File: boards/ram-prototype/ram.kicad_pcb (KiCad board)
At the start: 4 copper layers, 158 x 141 mm, 630 parts, among them J1 PinHeader_1x24_P2.54mm_Vertic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, J2 PinHeader_1x04_P2.54mm_Vertic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, J3 PinHeader_1x14_P2.54mm_Vertic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, J4 PinHeader_1x16_P2.54mm_Vertic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, J5 Molex_Mini-Fit_Jr_5566-08A_2x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, U1 DSBGA\-5_NumericPads, U10 DSBGA\-5_NumericPads, U100 DSBGA\-5_NumericPads, U101 DSBGA\-5_NumericPads, U102 DSBGA\-5_NumericPads, U103 DSBGA\-5_NumericPads, U104 DSBGA\-5_NumericPads, U105 DSBGA\-5_NumericPads, U106 DSBGA\-5_NumericPads, U107 DSBGA\-5_NumericPads, U108 DSBGA\-5_NumericPads, U109 DSBGA\-5_NumericPads, U11 DSBGA\-5_NumericPads, U110 DSBGA\-5_NumericPads, U111 DSBGA\-5_NumericPads, U112 DSBGA\-5_NumericPads, U113 DSBGA\-5_NumericPads, U114 DSBGA\-5_NumericPads, U115 DSBGA\-5_NumericPads, U116 DSBGA\-5_NumericPads, U117 DSBGA\-5_NumericPads, U118 DSBGA\-5_NumericPads, U119 DSBGA\-5_NumericPads, U12 DSBGA\-5_NumericPads, U120 DSBGA\-5_NumericPads, U121 DSBGA\-5_NumericPads, U122 DSBGA\-5_NumericPads, U123 DSBGA\-5_NumericPads, U124 DSBGA\-5_NumericPads, U125 DSBGA\-5_NumericPads, U126 DSBGA\-5_NumericPads, U127 DSBGA\-5_NumericPads, U128 DSBGA\-5_NumericPads, U129 DSBGA\-5_NumericPads, U13 DSBGA\-5_NumericPads, U130 DSBGA\-5_NumericPads, U131 DSBGA\-5_NumericPads, U132 DSBGA\-5_NumericPads, U133 DSBGA\-5_NumericPads, U134 DSBGA\-5_NumericPads, U135 DSBGA\-5_NumericPads, U136 DSBGA\-5_NumericPads, U137 DSBGA\-5_NumericPads, U138 DSBGA\-5_NumericPads, U139 DSBGA\-5_NumericPads, U14 DSBGA\-5_NumericPads, U140 DSBGA\-5_NumericPads, U141 DSBGA\-5_NumericPads, U142 DSBGA\-5_NumericPads, U143 DSBGA\-5_NumericPads, U144 DSBGA\-5_NumericPads, U145 DSBGA\-5_NumericPads, U146 DSBGA\-5_NumericPads, U147 DSBGA\-5_NumericPads, U148 DSBGA\-5_NumericPads, U149 DSBGA\-5_NumericPads, U15 DSBGA\-5_NumericPads, U150 DSBGA\-5_NumericPads, U151 DSBGA\-5_NumericPads, U152 DSBGA\-5_NumericPads, U153 DSBGA\-5_NumericPads, U154 DSBGA\-5_NumericPads, U155 DSBGA\-5_NumericPads, U156 DSBGA\-5_NumericPads, U157 DSBGA\-5_NumericPads, U158 DSBGA\-5_NumericPads, U159 DSBGA\-5_NumericPads, U16 DSBGA\-5_NumericPads, U160 DSBGA\-5_NumericPads, U161 DSBGA\-5_NumericPads, U162 DSBGA\-5_NumericPads, U163 DSBGA\-5_NumericPads, U164 DSBGA\-5_NumericPads, U165 DSBGA\-5_NumericPads, U166 DSBGA\-5_NumericPads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

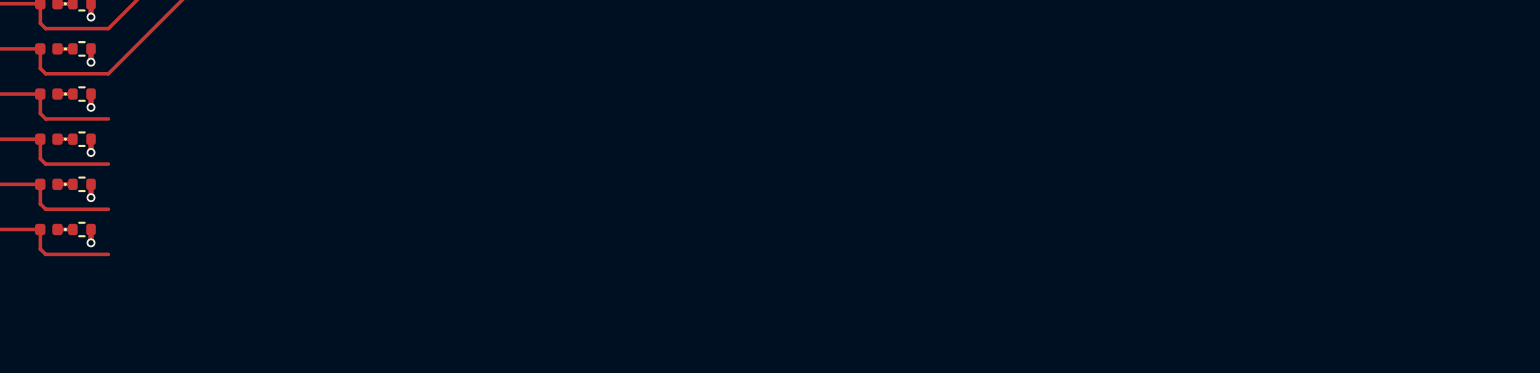
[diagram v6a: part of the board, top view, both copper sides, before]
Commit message: route A7-A10 column address bus from connector to column select
Add preroute_coladdr_to_colsel() that routes the 4 column address
signals (A7-A10) as a parallel horizontal bus from the connector
LED stubs to near the column_select inverter inputs on F.Cu.

The bus runs ~75mm horizontally at 2.54mm spacing (connector pitch)
through the clear corridor below the D* bus and byte grid. The
signal-to-INV mapping is reversed (A7→leftmost, A10→rightmost)
so a non-crossing 45° fan is impossible on a single layer — the
bus stops at the earliest peel-off point and the autorouter handles
the final ~12mm to each INV pin.

Also regenerates schematics to sync with latest generate_ram.py.

Co-Authored-By: Claude Opus 4.6 (1M context) <noreply@anthropic.com>
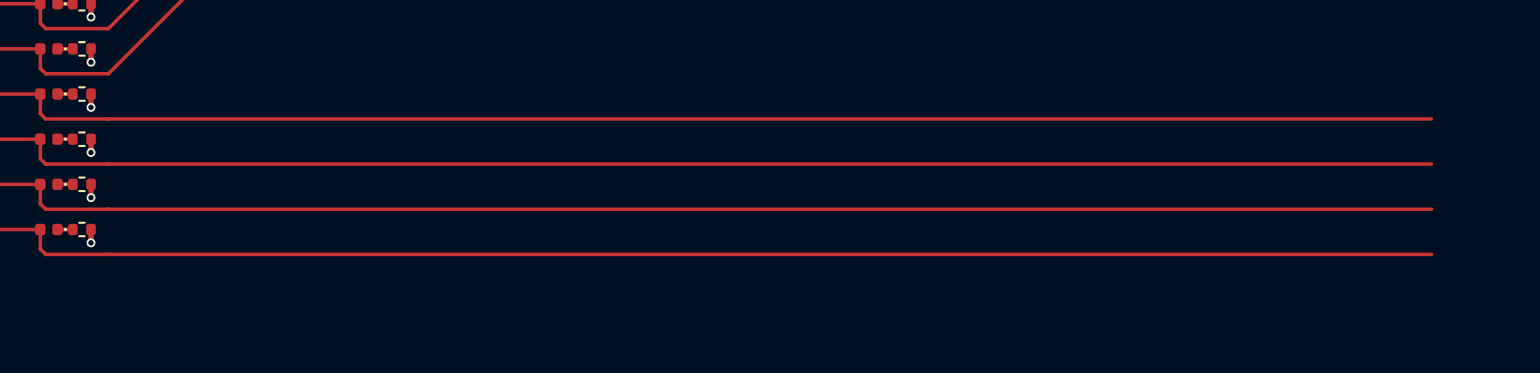
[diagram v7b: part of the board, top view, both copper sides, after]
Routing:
- net /Column Select/A9: track 11.6 -> 86.0 mm
- net /Column Select/A8: track 11.6 -> 86.0 mm
- net /Column Select/A7: track 11.6 -> 86.0 mm
- net /Column Select/A10: track 11.6 -> 86.0 mm
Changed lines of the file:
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@@
   (segment (start 65.54 125.02) (end 38.31 125.02) (width 0.2) (layer "F.Cu") (net 64))
   (segment (start 38.31 125.02) (end 30.35 132.98) (width 0.2) (layer "F.Cu") (net 64))
+  (segment (start 30.35 135.52) (end 104.78 135.52) (width 0.2) (layer "F.Cu") (net 55))
+  (segment (start 30.35 138.06) (end 104.78 138.06) (width 0.2) (layer "F.Cu") (net 54))
+  (segment (start 30.35 140.6) (end 104.78 140.6) (width 0.2) (layer "F.Cu") (net 53))
+  (segment (start 30.35 143.14) (end 104.78 143.14) (width 0.2) (layer "F.Cu") (net 52))
   (zone (net 91) (net_name "/Power Supply/+12V") (layer "F.Cu") (hatch edge 0.508)
     (priority 1)
